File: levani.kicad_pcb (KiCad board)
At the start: 2 copper layers, 85 x 55 mm, 11 parts, among them M1 Motor_DC, Q1 NPN, SW1 SW_Push

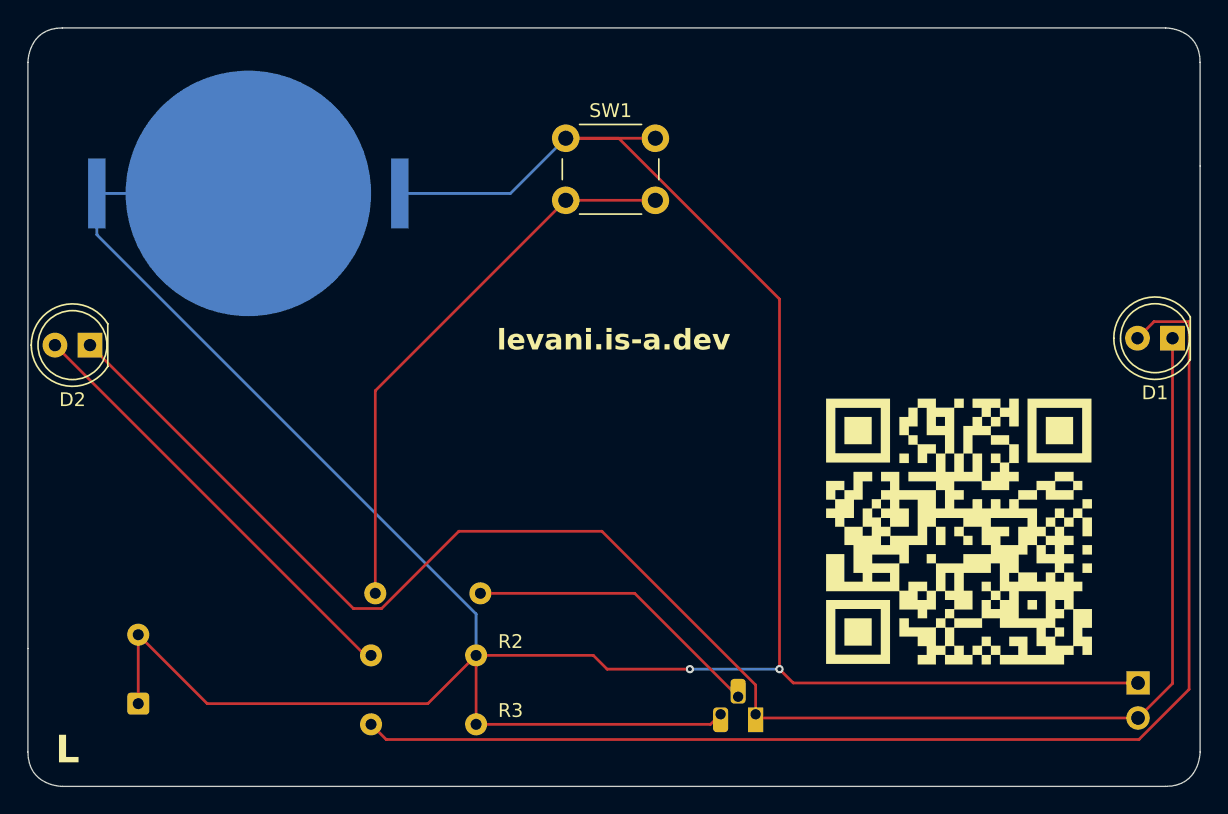
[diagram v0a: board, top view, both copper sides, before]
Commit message: fix schematic and add more silkscreened text
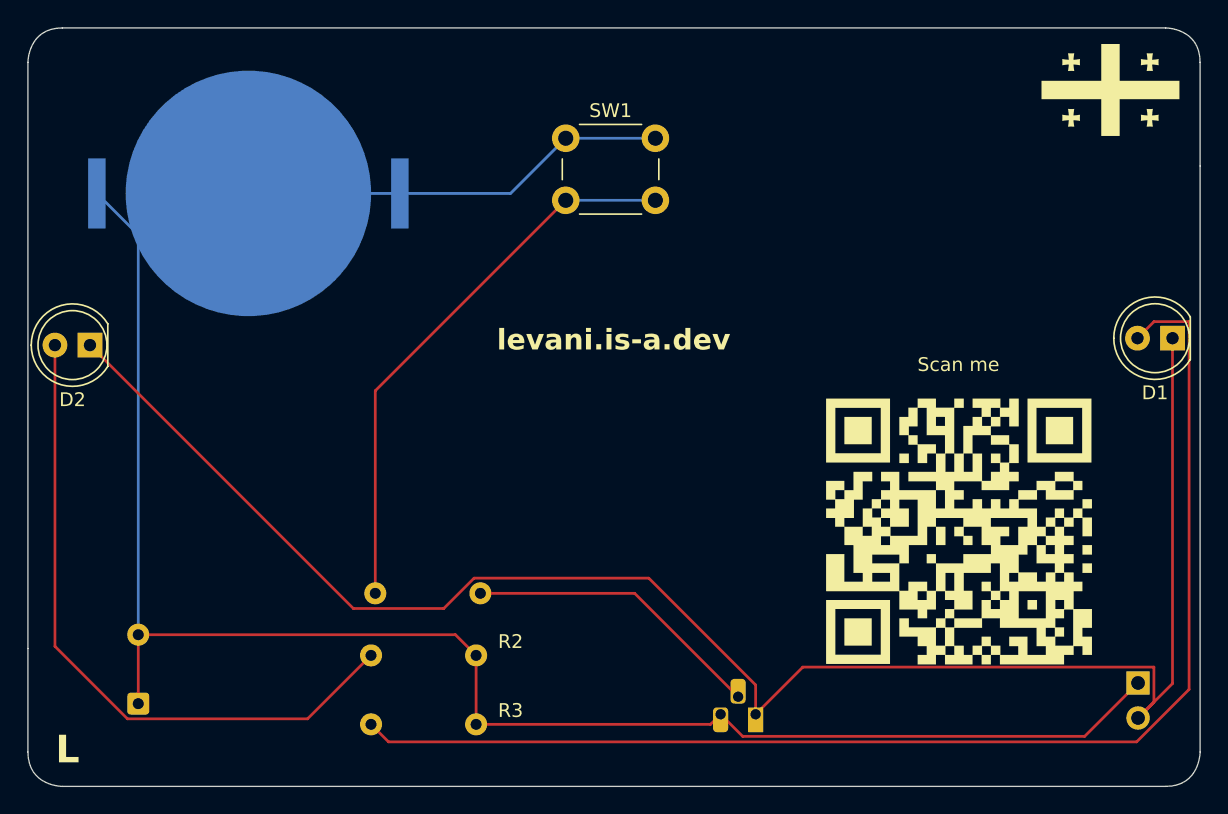
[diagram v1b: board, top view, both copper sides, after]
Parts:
- added G***: LOGO, LOGO, F.Cu at (150.0, 56.5)
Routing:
- net Net-(BT1-+): track 228.1 -> 150.1 mm, vias 2 -> 0
- net Net-(D2-A): track 32.2 -> 49.3 mm
- net Net-(D1-K): track 121.7 -> 125.8 mm
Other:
- board text added: "As part of the hackclub solder program"
- board text added: "Design Date: 21.06.2025"
- board text added: "Idk what this component does and at this point I am too afraid to ask"
- board text added: "Juice comes from here ->"
- board text added: "Motor go brrrr....."
- board text added: "Scan me"
- board text added: "Shine bright"
- board text added: "fancy shmancy capacitor"
- board text added: "like a diamond"
- board text added: "resisting the urge to add more text"
- board text added: "solder.hackclub.com"

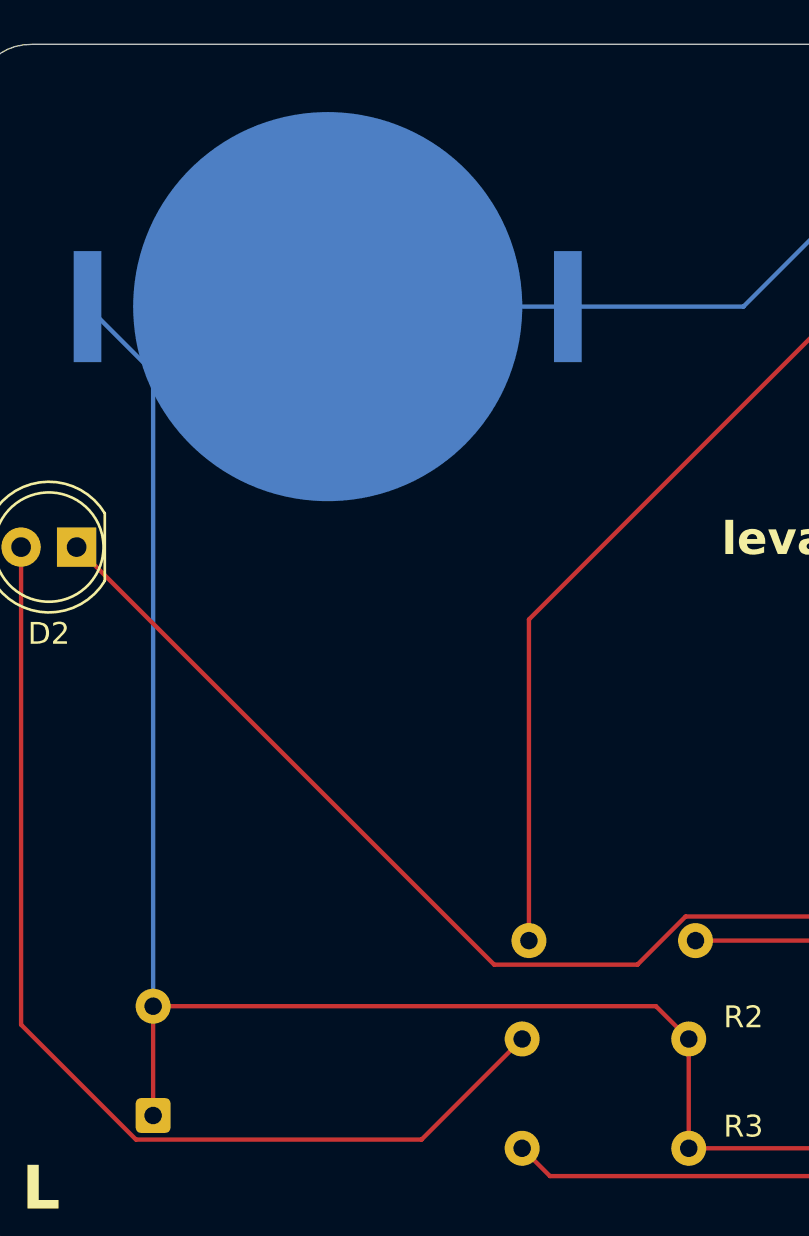
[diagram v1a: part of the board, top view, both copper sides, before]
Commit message: update schematic with more art
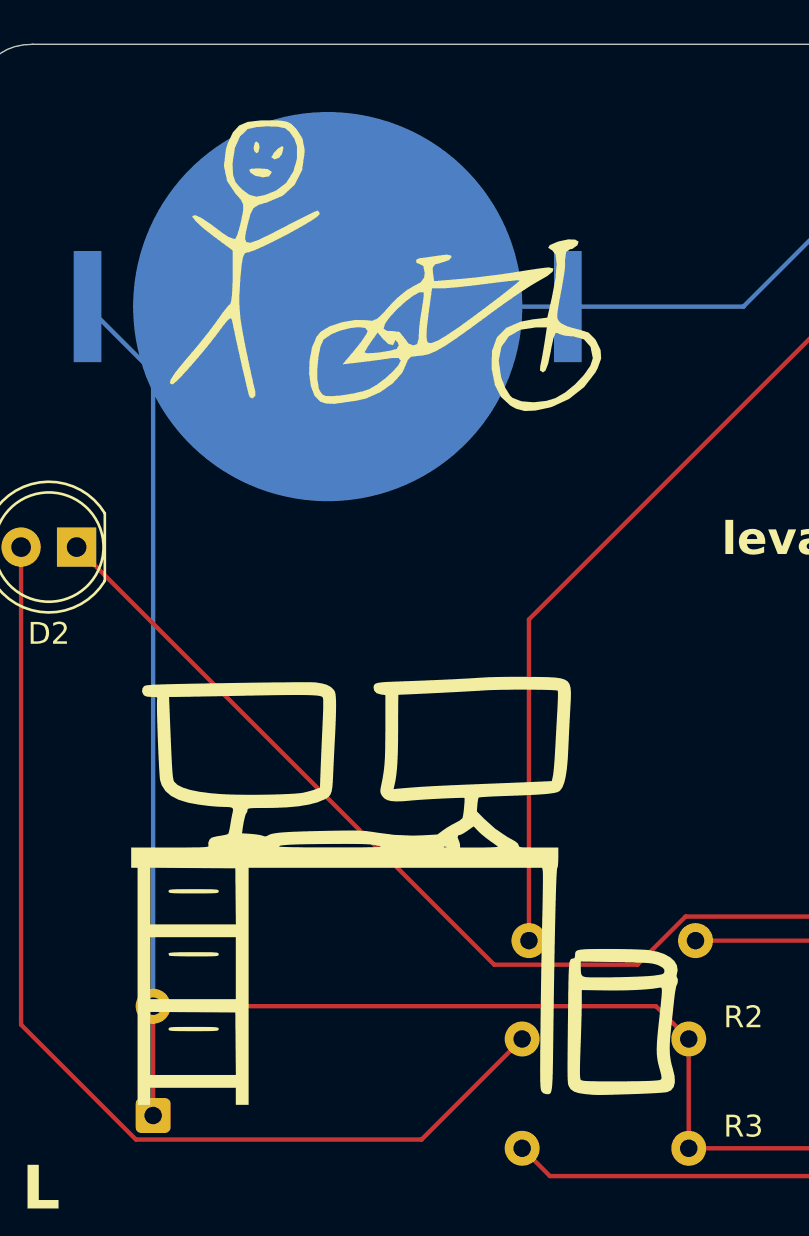
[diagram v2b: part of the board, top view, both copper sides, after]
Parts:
- added G***: LOGO, LOGO, F.Cu at (90.0, 62.0)
- added G***: LOGO, LOGO, F.Cu at (91.0, 90.5)
- added G***: LOGO, LOGO, B.Cu at (134.0, 95.0)
- added G***: LOGO, LOGO, B.Cu at (130.5, 74.0)

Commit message: Add files via upload
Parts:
- moved G*** 2.12 mm to (89.5, 92.0)
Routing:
- net (no net): vias 0 -> 1
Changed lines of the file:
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@@
 	(footprint "LOGO"
 		(layer "F.Cu")
-		(at 91 90.5)
+		(at 89.5 92)
 		(property "Reference" "G***"
 			(at 0 0 0)
@@
 			(at 8.485 9 0)
 			(layer "B.SilkS")
+			(hide yes)
 			(effects
 				(font
@@
 		)
 	)
+	(via
+		(at 75.5 55.5)
+		(size 5.5)
+		(drill 5)
+		(layers "F.Cu" "B.Cu")
+		(net 0)
+	)
 	(segment
